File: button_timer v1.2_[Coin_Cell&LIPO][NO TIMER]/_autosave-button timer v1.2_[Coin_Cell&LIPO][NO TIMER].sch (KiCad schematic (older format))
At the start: 23 parts, among them J1 Conn_01x05_Female, SW1 SW_Push, SW2 SW_Push, U1 TPS61097A, U2 AP2112K-3.3, X1 ESP-12E

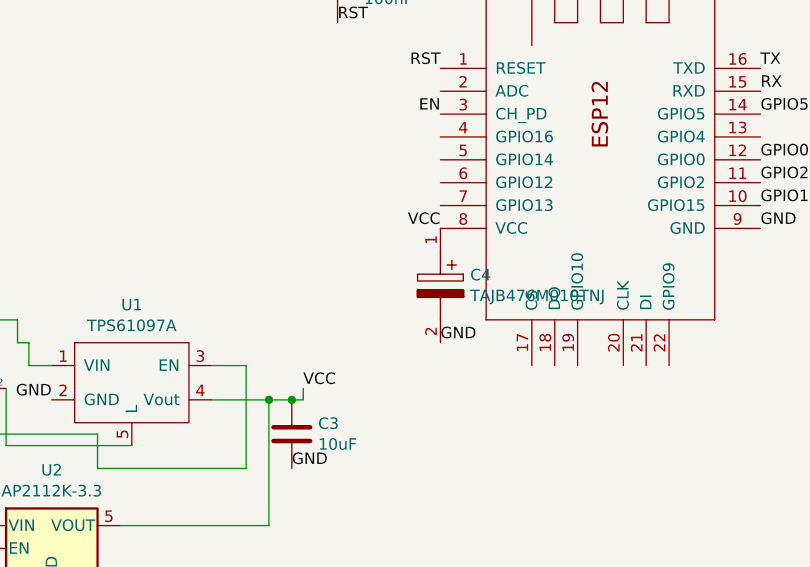
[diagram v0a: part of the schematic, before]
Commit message: Added 100nF decoupling capacitors between VCC and Ground of the ESP
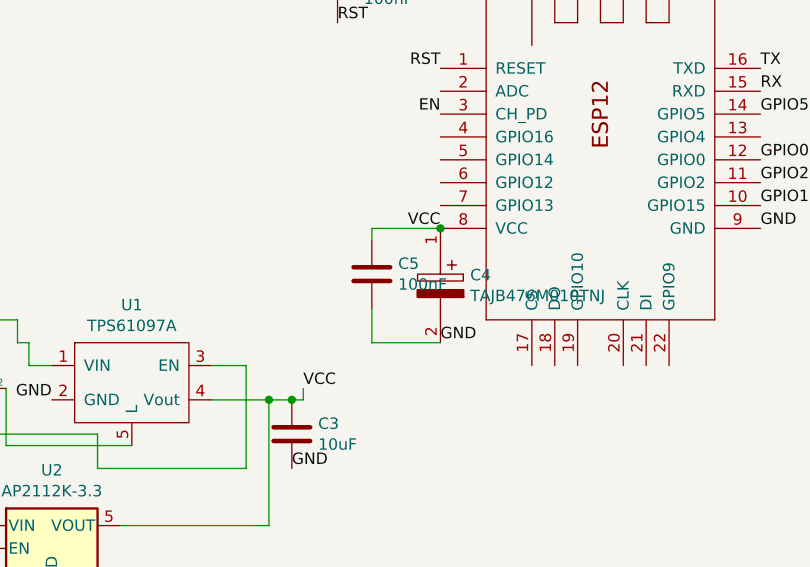
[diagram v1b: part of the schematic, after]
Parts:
- added C5: 100nF, handsolder:C_0402_1005Metric_Pad0.74x0.62mm_HandSoldermod, symbol Device:C
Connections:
- net GND: now also C5.2
- net VCC: now also C5.1
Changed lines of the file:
@@
 Text Label 5300 4200 0    50   ~ 0
 GND
+$Comp
+L Device:C C5
+U 1 1 60368135
+P 5000 3900
+F 0 "C5" H 5115 3946 50  0000 L CNN
+F 1 "100nF" H 5115 3855 50  0000 L CNN
+F 2 "handsolder:C_0402_1005Metric_Pad0.74x0.62mm_HandSoldermod" H 5038 3750 50  0001 C CNN
+F 3 "~" H 5000 3900 50  0001 C CNN
+	1    5000 3900
+	1    0    0    -1
+$EndComp
+Wire Wire Line
+	5000 3750 5000 3700
+Wire Wire Line
+	5000 3700 5300 3700
+Connection ~ 5300 3700
+Wire Wire Line
+	5000 4050 5000 4200
+Wire Wire Line
+	5000 4200 5300 4200
 $EndSCHEMATC
